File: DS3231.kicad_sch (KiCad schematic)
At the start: 12 parts, among them IC1 DS3231/SO

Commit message: added drawing sheet
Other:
- title: (none) -> DS3231
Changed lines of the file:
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@@
 	(generator_version "8.0")
 	(paper "A4")
+	(title_block
+		(title "DS3231")
+		(date "2024-03-06")
+	)
 	(wire
 		(pts

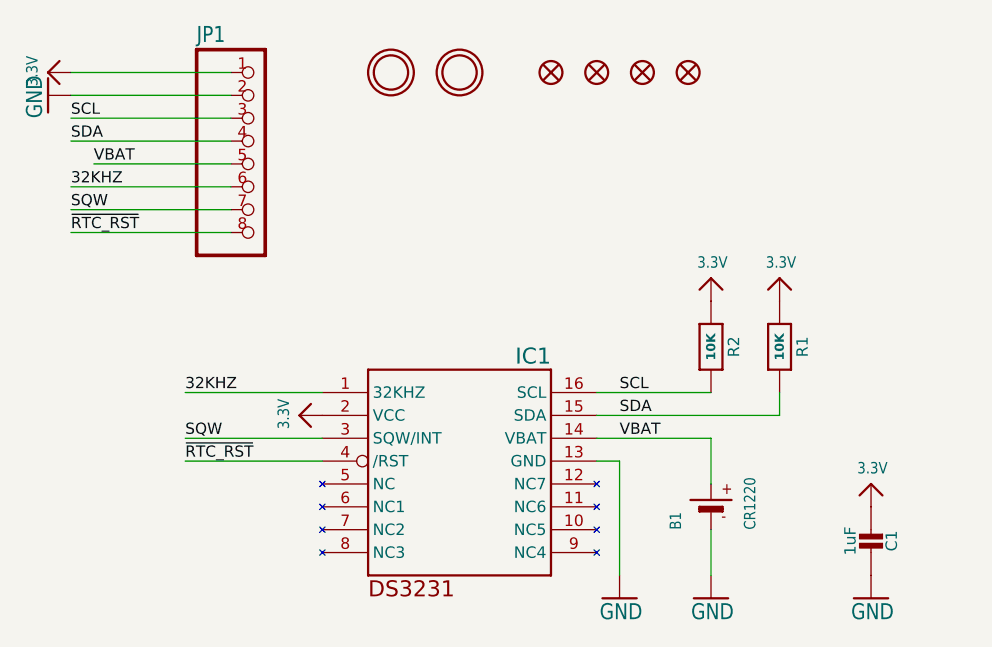
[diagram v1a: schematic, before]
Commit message: fully migrated to KiCad
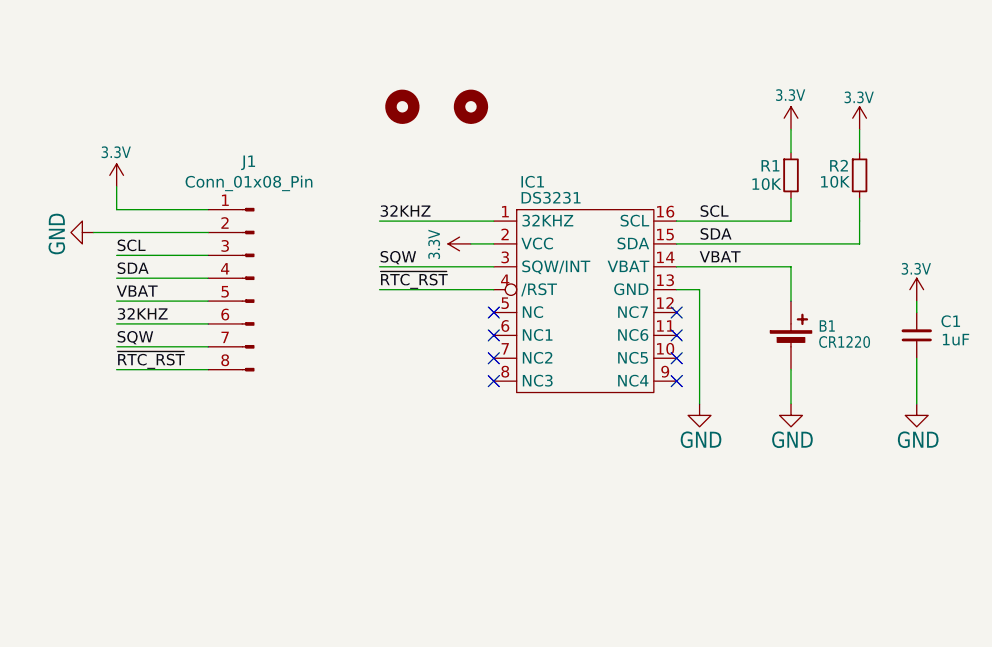
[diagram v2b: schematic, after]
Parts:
- removed B1: CR1220, DS3231:CR1220, symbol DS3231-eagle-import:BATTERYCR1220_SMT
- removed C1: 1uF, DS3231:0805-NO, symbol DS3231-eagle-import:CAP_CERAMIC0805-NOOUTLINE
- removed FID1, FID2, FID3, FID4: FIDUCIAL{dblquote}{dblquote}, DS3231:FIDUCIAL_1MM, symbol DS3231-eagle-import:FIDUCIAL{dblquote}{dblquote}
- removed IC1: DS3231/SO, DS3231:SO16W, symbol DS3231-eagle-import:DS3231/SO
- removed JP1: HEADER-1X870MIL, DS3231:1X08_ROUND_70, symbol DS3231-eagle-import:HEADER-1X870MIL
- removed R1, R2: 10K, DS3231:0805-NO, symbol DS3231-eagle-import:RESISTOR0805_NOOUTLINE
- removed U$6, U$7: MOUNTINGHOLE2.5, DS3231:MOUNTINGHOLE_2.5_PLATED, symbol DS3231-eagle-import:MOUNTINGHOLE2.5
- added B1: CR1220, external_footprints:CR1220-SMD, symbol Device:Battery_Cell
- added C1: 1uF, Capacitor_SMD:C_0805_2012Metric, symbol Device:C_Small
- added IC1: DS3231, Package_SO:SOIC-16W_7.5x10.3mm_P1.27mm, symbol external_library:DS3231
- added J1: Conn_01x08_Pin, Connector_PinHeader_2.54mm:PinHeader_1x08_P2.54mm_Vertical, symbol Connector:Conn_01x08_Pin
- added R1, R2: 10K, Resistor_SMD:R_0805_2012Metric, symbol Device:R_Small
- added U$1, U$2: MOUNTINGHOLE2.5, MountingHole:MountingHole_2.5mm, symbol Mechanical:MountingHole
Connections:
- net 3.3V: now also C1.2, IC1.2 (VCC), J1.1 (Pin_1), R1.1, R2.1
- net 32KHZ: now also IC1.1 (32KHZ), J1.6 (Pin_6)
- net GND: now also B1.2 (-), C1.1, IC1.13 (GND), J1.2 (Pin_2)
- net SCL: now also IC1.16 (SCL), J1.3 (Pin_3), R1.2
- net SDA: now also IC1.15 (SDA), J1.4 (Pin_4), R2.2
- net SQW: now also IC1.3 (SQW/INT), J1.7 (Pin_7)
- net VBAT: now also B1.1 (+), IC1.14 (VBAT), J1.5 (Pin_5)
- net ~{RTC_RST}: now also IC1.4 (/RST), J1.8 (Pin_8)
- no-connect marks 0 -> 8

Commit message: added info to generate BOM file
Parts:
- B1: Component package type (none) -> /; MPN (none) -> 3001; Manufacturer (none) -> Keystone Electronics; SPN (none) -> 36-3001-ND; Supplier (none) -> DigiKey
- C1: Component package type (none) -> C_0805; MPN (none) -> /; Manufacturer (none) -> /; SPN (none) -> GPC0805105; Supplier (none) -> Eurocircuits
- IC1: Component package type (none) -> /; MPN (none) -> DS3231M+TRL; Manufacturer (none) -> Analog Devices Inc./Maxim Integrated; SPN (none) -> DS3231M+TRLTR-ND - Tape & Reel (TR); Supplier (none) -> DigiKey
- J1: Component package type (none) -> /; MPN (none) -> SSQ-108-01-G-S; Manufacturer (none) -> Samtec Inc.; SPN (none) -> SAM1180-08-ND; Supplier (none) -> DigiKey
- R1, R2: Component package type (none) -> R_0805; MPN (none) -> /; Manufacturer (none) -> /; SPN (none) -> GPR080510K; Supplier (none) -> Eurocircuits
- U$1, U$2: now left out of the parts list

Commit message: fixed incorrect item in BOM
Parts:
- J1: MPN SSQ-108-01-G-S -> TSW-108-23-G-S; SPN SAM1180-08-ND -> 612-TSW-108-23-G-S-ND
- R1, R2: value 10K -> 10k
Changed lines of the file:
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@@
 			)
 		)
-		(property "Value" "10K"
+		(property "Value" "10k"
 			(at 188.976 88.392 0)
 			(effects
@@
 			)
 		)
-		(property "Datasheet" "~"
+		(property "Datasheet" ""
 			(at 148.59 80.01 0)
 			(effects
@@
 			)
 		)
-		(property "Datasheet" "~"
+		(property "Datasheet" ""
 			(at 140.97 80.01 0)
 			(effects
@@
 			)
 		)
-		(property "Description" "CONN RCPT 8POS 0.1 GOLD PCB"
+		(property "Description" "CONN HEADER VERT 8POS 2.54MM"
 			(at 124.46 99.06 0)
 			(effects
@@
 			)
 		)
-		(property "MPN" "SSQ-108-01-G-S"
+		(property "MPN" "TSW-108-23-G-S"
 			(at 124.46 99.06 0)
 			(effects
@@
 			)
 		)
-		(property "SPN" "SAM1180-08-ND"
+		(property "SPN" "612-TSW-108-23-G-S-ND"
 			(at 124.46 99.06 0)
 			(effects
@@
 			)
 		)
-		(property "Value" "10K"
+		(property "Value" "10k"
 			(at 181.356 88.646 0)
 			(effects

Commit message: updated routing + symbol update
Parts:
- B1: now left out of the parts list
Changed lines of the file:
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@@
 	)
 	(no_connect
-		(at 151.13 107.95)
+		(at 148.59 107.95)
 	)
 	(no_connect
@@
 	)
 	(no_connect
-		(at 151.13 110.49)
+		(at 148.59 110.49)
 	)
 	(no_connect
-		(at 151.13 105.41)
+		(at 148.59 105.41)
 	)
 	(no_connect
@@
 	)
 	(no_connect
-		(at 151.13 102.87)
+		(at 148.59 102.87)
 	)
 	(no_connect
@@
 	(wire
 		(pts
-			(xy 138.43 100.33) (xy 151.13 100.33)
+			(xy 135.89 100.33) (xy 148.59 100.33)
 		)
 		(stroke
@@
 	(wire
 		(pts
-			(xy 138.43 92.71) (xy 151.13 92.71)
+			(xy 135.89 92.71) (xy 148.59 92.71)
 		)
 		(stroke
@@
 	(wire
 		(pts
-			(xy 148.59 95.25) (xy 151.13 95.25)
+			(xy 147.32 95.25) (xy 148.59 95.25)
 		)
 		(stroke
@@
 	(wire
 		(pts
-			(xy 138.43 97.79) (xy 151.13 97.79)
+			(xy 135.89 97.79) (xy 148.59 97.79)
 		)
 		(stroke
@@
 	)
 	(label "SQW"
-		(at 138.43 97.79 0)
+		(at 135.89 97.79 0)
 		(fields_autoplaced yes)
 		(effects
@@
 	)
 	(label "32KHZ"
-		(at 138.43 92.71 0)
+		(at 135.89 92.71 0)
 		(fields_autoplaced yes)
 		(effects
@@
 	)
 	(label "~{RTC_RST}"
-		(at 138.43 100.33 0)
+		(at 135.89 100.33 0)
 		(fields_autoplaced yes)
 		(effects
@@
 	(symbol
 		(lib_id "power:+3.3V")
-		(at 148.59 95.25 90)
+		(at 147.32 95.25 90)
 		(unit 1)
 		(exclude_from_sim no)
@@
 		(dnp no)
 		(property "Reference" "#U$02"
-			(at 148.59 95.25 0)
+			(at 147.32 95.25 0)
 			(effects
 				(font
@@
 		)
 		(property "Value" "3.3V"
-			(at 145.288 97.028 0)
+			(at 144.526 94.488 90)
 			(effects
 				(font
@@
 		)
 		(property "Footprint" ""
-			(at 148.59 95.25 0)
+			(at 147.32 95.25 0)
 			(effects
 				(font
@@
 		)
 		(property "Datasheet" ""
-			(at 148.59 95.25 0)
+			(at 147.32 95.25 0)
 			(effects
 				(font
@@
 		)
 		(property "Description" "Power symbol creates a global label with name \"+3.3V\""
-			(at 148.59 95.25 0)
+			(at 147.32 95.25 0)
 			(effects
 				(font
@@
 		(unit 1)
 		(exclude_from_sim no)
-		(in_bom yes)
+		(in_bom no)
 		(on_board yes)
 		(dnp no)
@@
 				(path "/3054a26c-491b-4a2c-bd9e-2e89ff40ccf1"
 					(reference "B1")
+					(unit 1)
+				)
+			)
+		)
+	)
+	(symbol
+		(lib_id "external_library:DS3231")
+		(at 152.4 111.76 0)
+		(unit 1)
+		(exclude_from_sim no)
+		(in_bom yes)
+		(on_board yes)
+		(dnp no)
+		(property "Reference" "IC1"
+			(at 154.178 88.392 0)
+			(effects
+				(font
+					(size 1.27 1.27)
+				)
+			)
+		)
+		(property "Value" "DS3231"
+			(at 156.21 90.17 0)
+			(effects
+				(font
+					(size 1.27 1.27)
+				)
+			)
+		)
+		(property "Footprint" "Package_SO:SOIC-16W_7.5x10.3mm_P1.27mm"
+			(at 162.306 114.808 0)
+			(effects
+				(font
+					(size 1.27 1.27)
+				)
+				(hide yes)
+			)
+		)
+		(property "Datasheet" ""
+			(at 149.86 92.71 0)
+			(effects
+				(font
+					(size 1.27 1.27)
+				)
+				(hide yes)
+			)
+		)
+		(property "Description" "IC RTC CLK/CALENDAR I2C 16SOIC"
+			(at 149.86 92.71 0)
+			(effects
+				(font
+					(size 1.27 1.27)
+				)
+				(hide yes)
+			)
+		)
+		(property "Manufacturer" "Analog Devices Inc./Maxim Integrated"
+			(at 152.4 111.76 0)
+			(effects
+				(font
+					(size 1.27 1.27)
+				)
+				(hide yes)
+			)
+		)
+		(property "MPN" "DS3231M+TRL"
+			(at 152.4 111.76 0)
+			(effects
+				(font
+					(size 1.27 1.27)
+				)
+				(hide yes)
+			)
+		)
+		(property "Supplier" "DigiKey"
+			(at 152.4 111.76 0)
+			(effects
+				(font
+					(size 1.27 1.27)
+				)
+				(hide yes)
+			)
+		)
+		(property "SPN" "DS3231M+TRLTR-ND - Tape & Reel (TR)"
+			(at 152.4 111.76 0)
+			(effects
+				(font
+					(size 1.27 1.27)
+				)
+				(hide yes)
+			)
+		)
+		(property "Component package type" "/"
+			(at 152.4 111.76 0)
+			(effects
+				(font
+					(size 1.27 1.27)
+				)
+				(hide yes)
+			)
+		)
+		(pin "1"
+		)
+		(pin "10"
+		)
+		(pin "15"
+		)
+		(pin "14"
+		)
+		(pin "5"
+		)
+		(pin "8"
+		)
+		(pin "12"
+		)
+		(pin "7"
+		)
+		(pin "9"
+		)
+		(pin "6"
+		)
+		(pin "2"
+		)
+		(pin "3"
+		)
+		(pin "13"
+		)
+		(pin "11"
+		)
+		(pin "16"
+		)
+		(pin "4"
+		)
+		(instances
+			(project "DS3231"
+				(path "/3054a26c-491b-4a2c-bd9e-2e89ff40ccf1"
+					(reference "IC1")
 					(unit 1)
 				)
@@
 	)
 	(symbol
-		(lib_id "external_library:DS3231")
-		(at 153.67 111.76 0)
-		(unit 1)
-		(exclude_from_sim no)
-		(in_bom yes)
-		(on_board yes)
-		(dnp no)
-		(property "Reference" "IC1"
-			(at 155.448 88.392 0)
-			(effects
-				(font
-					(size 1.27 1.27)
-				)
-			)
-		)
-		(property "Value" "DS3231"
-			(at 157.48 90.17 0)
-			(effects
-				(font
-					(size 1.27 1.27)
-				)
-			)
-		)
-		(property "Footprint" "Package_SO:SOIC-16W_7.5x10.3mm_P1.27mm"
-			(at 163.576 114.808 0)
-			(effects
-				(font
-					(size 1.27 1.27)
-				)
-				(hide yes)
-			)
-		)
-		(property "Datasheet" ""
-			(at 151.13 92.71 0)
-			(effects
-				(font
-					(size 1.27 1.27)
-				)
-				(hide yes)
-			)
-		)
-		(property "Description" "IC RTC CLK/CALENDAR I2C 16SOIC"
-			(at 151.13 92.71 0)
-			(effects
-				(font
-					(size 1.27 1.27)
-				)
-				(hide yes)
-			)
-		)
-		(property "Manufacturer" "Analog Devices Inc./Maxim Integrated"
-			(at 153.67 111.76 0)
-			(effects
-				(font
-					(size 1.27 1.27)
-				)
-				(hide yes)
-			)
-		)
-		(property "MPN" "DS3231M+TRL"
-			(at 153.67 111.76 0)
-			(effects
-				(font
-					(size 1.27 1.27)
-				)
-				(hide yes)
-			)
-		)
-		(property "Supplier" "DigiKey"
-			(at 153.67 111.76 0)
-			(effects
-				(font
-					(size 1.27 1.27)
-				)
-				(hide yes)
-			)
-		)
-		(property "SPN" "DS3231M+TRLTR-ND - Tape & Reel (TR)"
-			(at 153.67 111.76 0)
-			(effects
-				(font
-					(size 1.27 1.27)
-				)
-				(hide yes)
-			)
-		)
-		(property "Component package type" "/"
-			(at 153.67 111.76 0)
-			(effects
-				(font
-					(size 1.27 1.27)
-				)
-				(hide yes)
-			)
-		)
-		(pin "1"
-		)
-		(pin "10"
-		)
-		(pin "15"
-		)
-		(pin "14"
-		)
-		(pin "5"
-		)
-		(pin "8"
-		)
-		(pin "12"
-		)
-		(pin "7"
-		)
-		(pin "9"
-		)
-		(pin "6"
-		)
-		(pin "2"
-		)
-		(pin "3"
-		)
-		(pin "13"
-		)
-		(pin "11"
-		)
-		(pin "16"
-		)
-		(pin "4"
-		)
-		(instances
-			(project "DS3231"
-				(path "/3054a26c-491b-4a2c-bd9e-2e89ff40ccf1"
-					(reference "IC1")
-					(unit 1)
-				)
-			)
-		)
-	)
-	(symbol
 		(lib_id "power:+3.3V")
 		(at 109.22 88.9 0)
@@
 		(dnp no)
 		(property "Reference" "J1"
-			(at 123.952 86.106 0)
+			(at 123.952 86.868 0)
 			(effects
 				(font
@@
 					(size 1.27 1.27)
 				)
-			)
-		)
+				(hide yes)
+			)
+		)

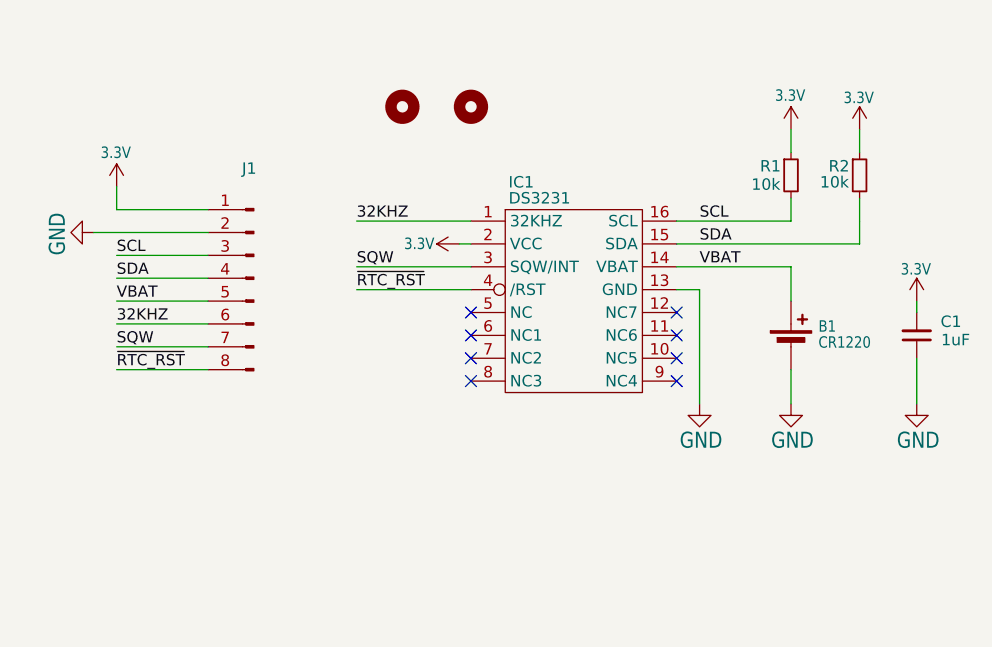
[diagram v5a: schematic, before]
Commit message: CR1220 footprint update
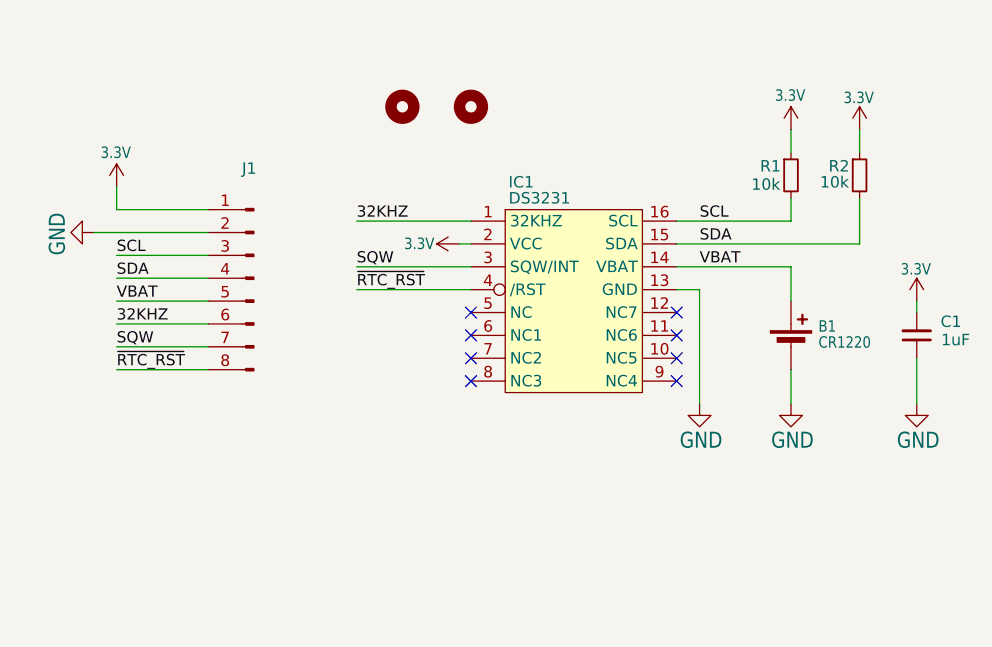
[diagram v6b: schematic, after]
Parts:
- B1: footprint external_footprints:CR1220-SMD -> external_footprints:CR1220
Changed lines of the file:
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@@
 			)
 		)
-		(property "Footprint" "external_footprints:CR1220-SMD"
+		(property "Footprint" "external_footprints:CR1220"
 			(at 184.15 105.156 90)
 			(effects

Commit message: BOM presets update
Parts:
- B1, J1: Component package type / -> (none)
- C1: Component package type C_0805 -> (none)
- IC1: Component package type / -> (none); SPN DS3231M+TRLTR-ND - Tape & Reel (TR) -> DS3231M+TRLTR-ND
- R1, R2: Component package type R_0805 -> (none)
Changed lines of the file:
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@@
-			)
-		)
-		(property "Component package type" "/"
-			(at 184.15 106.68 0)
-			(effects
-				(font
-					(size 1.27 1.27)
-				)
-				(hide yes)
 			)
 		)
@@
 			)
 		)
-		(property "SPN" "DS3231M+TRLTR-ND - Tape & Reel (TR)"
-			(at 152.4 111.76 0)
-			(effects
-				(font
-					(size 1.27 1.27)
-				)
-				(hide yes)
-			)
-		)
-		(property "Component package type" "/"
+		(property "SPN" "DS3231M+TRLTR-ND"
 			(at 152.4 111.76 0)
 			(effects
@@
 			)
 		)
-		(property "Component package type" "R_0805"
-			(at 191.77 87.63 0)
-			(effects
-				(font
-					(size 1.27 1.27)
-				)
-				(hide yes)
-			)
-		)
 		(pin "1"
 		)
@@
 			)
 		)
-		(property "Component package type" "C_0805"
-			(at 198.12 105.41 0)
-			(effects
-				(font
-					(size 1.27 1.27)
-				)
-				(hide yes)
-			)
-		)
 		(pin "1"
 		)
@@
 			)
 		)
-		(property "Component package type" "/"
-			(at 124.46 99.06 0)
-			(effects
-				(font
-					(size 1.27 1.27)
-				)
-				(hide yes)
-			)
-		)
 		(pin "1"
 		)
@@
 			(at 184.15 87.63 0)
 			(effects
-				(font
-					(size 1.27 1.27)
-				)
-				(hide yes)
-			)
-		)
-		(property "Component package type" "R_0805"
-			(at 184.15 87.63 0)
-			(effects
